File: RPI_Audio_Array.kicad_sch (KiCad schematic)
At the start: 74 parts, among them J1 Conn_02x20_Odd_Even, U1 PCMD3140IRTER, U2 SPH0690LM4H-1, U3 SPH0690LM4H-1, U4 SPH0690LM4H-1, U5 SPH0690LM4H-1, U6 TLV7103318QDSERQ1

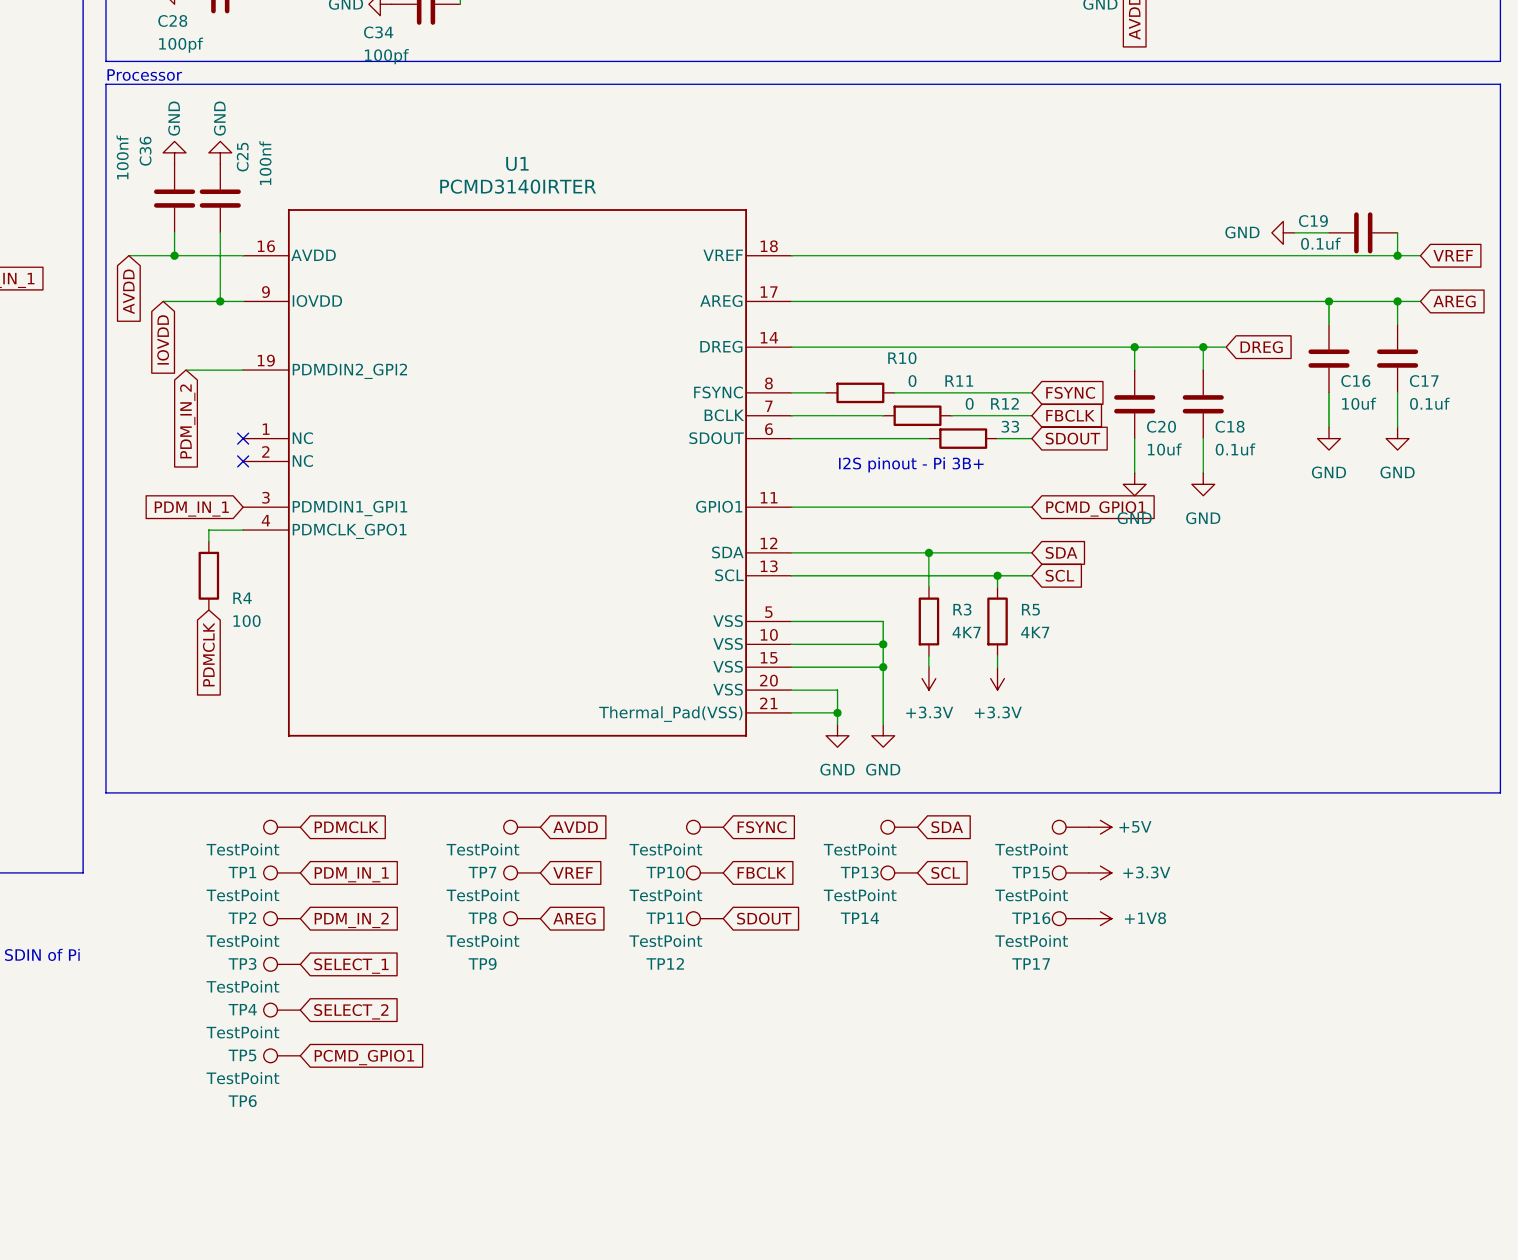
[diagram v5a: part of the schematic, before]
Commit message: Feat: Resolving all DRC warnings
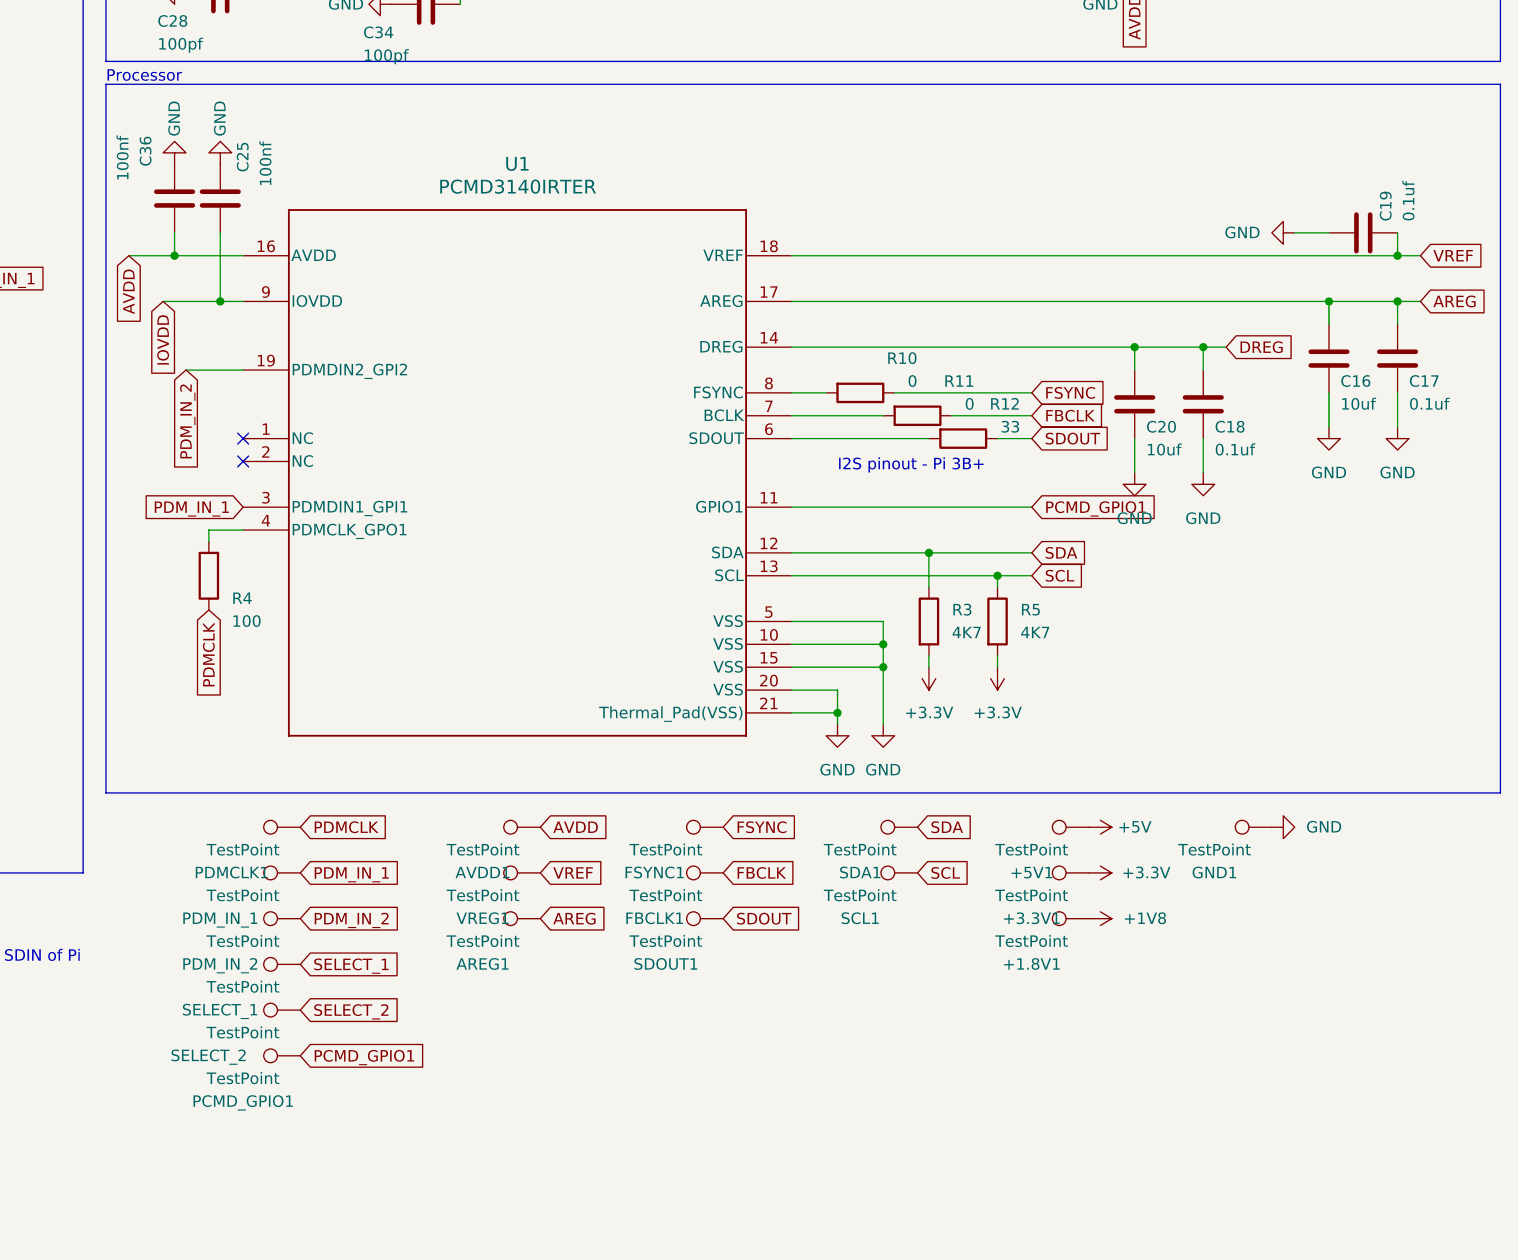
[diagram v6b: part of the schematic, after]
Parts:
- added GND1: TestPoint, TestPoint:TestPoint_Plated_Hole_D2.0mm, symbol Connector:TestPoint
- C13, C32: footprint Capacitor_SMD:C_01005_0402Metric -> Capacitor_SMD:C_0805_2012Metric; lcsc CL05B103KB5NNNC -> CL21B103KBANNNC
- C19: footprint Capacitor_SMD:C_01005_0402Metric -> Capacitor_SMD:C_0603_1608Metric; lcsc CL05B104KB54PNC -> CC0603KRX7R9BB104
- renumbered TP17 to +1.8V1, TP16 to +3.3V1, TP15 to +5V1, TP9 to AREG1, TP7 to AVDD1, TP11 to FBCLK1, TP10 to FSYNC1, TP6 to PCMD_GPIO1, TP1 to PDMCLK1, TP2 to PDM_IN_1, TP3 to PDM_IN_2, TP14 to SCL1, TP13 to SDA1, TP12 to SDOUT1, TP4 to SELECT_1, TP5 to SELECT_2, TP8 to VREG1
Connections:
- net GND: now also GND1.1

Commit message: updated PCB and schematic for review
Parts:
- removed +1.8V1, +3.3V1, +5V1, AREG1, AVDD1, FBCLK1, FSYNC1, GND1, PCMD_GPIO1, PDMCLK1, PDM_IN_1, PDM_IN_2, SCL1, SDA1, SDOUT1, SELECT_1, SELECT_2, VREG1: TestPoint, TestPoint:TestPoint_Plated_Hole_D2.0mm, symbol Connector:TestPoint
- removed C36: 100nf, Capacitor_SMD:C_1206_3216Metric, symbol Device:C
- added C35: 100nF, Capacitor_SMD:C_0603_1608Metric, symbol Device:C
- added H1, H2: MountingHole, MountingHole:MountingHole_2.7mm_M2.5, symbol Mechanical:MountingHole
- added TP1: PDMCLK, TestPoint:TestPoint_Plated_Hole_D2.0mm, symbol Connector:TestPoint
- added TP10: FSYNC, TestPoint:TestPoint_Plated_Hole_D2.0mm, symbol Connector:TestPoint
- added TP11: FBCLK, TestPoint:TestPoint_Plated_Hole_D2.0mm, symbol Connector:TestPoint
- added TP12: SDOUT, TestPoint:TestPoint_Plated_Hole_D2.0mm, symbol Connector:TestPoint
- added TP13: SDA, TestPoint:TestPoint_Plated_Hole_D2.0mm, symbol Connector:TestPoint
- added TP14: SCL, TestPoint:TestPoint_Plated_Hole_D2.0mm, symbol Connector:TestPoint
- added TP15: 5V, TestPoint:TestPoint_Plated_Hole_D2.0mm, symbol Connector:TestPoint
- added TP16: 3V3, TestPoint:TestPoint_Plated_Hole_D2.0mm, symbol Connector:TestPoint
- added TP17: 1V8, TestPoint:TestPoint_Plated_Hole_D2.0mm, symbol Connector:TestPoint
- added TP18: GND, TestPoint:TestPoint_Plated_Hole_D2.0mm, symbol Connector:TestPoint
- added TP19: PDMVDD3, TestPoint:TestPoint_Plated_Hole_D2.0mm, symbol Connector:TestPoint
- added TP2: PDMIN1, TestPoint:TestPoint_Plated_Hole_D2.0mm, symbol Connector:TestPoint
- added TP20: PDMVDD4, TestPoint:TestPoint_Plated_Hole_D2.0mm, symbol Connector:TestPoint
- added TP3: PDMIN2, TestPoint:TestPoint_Plated_Hole_D2.0mm, symbol Connector:TestPoint
- added TP4, TP5: PDMVDD2, TestPoint:TestPoint_Plated_Hole_D2.0mm, symbol Connector:TestPoint
- added TP6: PCM_IO1, TestPoint:TestPoint_Plated_Hole_D2.0mm, symbol Connector:TestPoint
- added TP8: VREF, TestPoint:TestPoint_Plated_Hole_D2.0mm, symbol Connector:TestPoint
- added TP9: AREG, TestPoint:TestPoint_Plated_Hole_D2.0mm, symbol Connector:TestPoint
- C1, C17, C18, C19, C2, C4, C6: value 0.1uf -> 100nF; lcsc CC0603KRX7R9BB104 -> C14663
- C10, C3, C7, C9: value 47pf -> 47pF; lcsc CL10C470JB8NNNC -> C1671
- C11, C12, C5, C8: value 330pf -> 330pF; lcsc CL10C331JB8NNNC -> C1664
- C13, C32: value 10nf -> 10nF; footprint Capacitor_SMD:C_0805_2012Metric -> Capacitor_SMD:C_0603_1608Metric; lcsc CL21B103KBANNNC -> C57112
- C14, C15: value 1uf -> 1uF; lcsc CL10A105KB8NNNC -> C15849
- C16, C20: value 10uf -> 10uF; lcsc CL21A106KAYNNNE -> C440198
- C21, C22, C23, C24: value 2.2uf -> 2.2uF; lcsc CL21A225KBQNNNE -> C377773
- C25, C26, C31: value 100nf -> 100nF; footprint Capacitor_SMD:C_1206_3216Metric -> Capacitor_SMD:C_0603_1608Metric; lcsc CL31B104KBCNNNC -> C14663
- C27, C33: value 1nf -> 1nF; footprint Capacitor_SMD:C_0805_2012Metric -> Capacitor_SMD:C_0603_1608Metric; lcsc CL21B102KBCNNNC -> C1588
- C28, C34: value 100pf -> 100pF; footprint Capacitor_SMD:C_0805_2012Metric -> Capacitor_SMD:C_0603_1608Metric; lcsc CL21C101JBANNNC -> C14858
- C29, C30: value 10uf -> 10uF; lcsc CL31A106KBHNNNE -> C13585
- FB1, FB2, FB3, FB4, FB5: footprint Capacitor_SMD:C_0805_2012Metric -> Inductor_SMD:L_0805_2012Metric; lcsc GZ2012D601TF -> C1017
- J1: lcsc (none) -> DNP
- R1, R2, R4, R8, R9: value 100 -> 100Ω; footprint Resistor_SMD:R_1206_3216Metric -> Resistor_SMD:R_0603_1608Metric; lcsc 1206W4F1000T5E -> C22775
- R10, R11: value 0 -> 0Ω; footprint Resistor_SMD:R_1206_3216Metric -> Resistor_SMD:R_0603_1608Metric; lcsc 1206W4F0000T5E -> C21189
- R12: value 33 -> 33Ω; footprint Resistor_SMD:R_0805_2012Metric -> Resistor_SMD:R_0603_1608Metric; lcsc 0805W8F330JT5E -> C23140
- R3, R5: value 4K7 -> 4K7Ω; lcsc 0603WAF4701T5E -> C23162
- U1: footprint RTE0020A-MFG -> Audio_Break_Out:RTE0020A-MFG; lcsc (none) -> DNP (Not Available)
- U2, U3, U4, U5: footprint SPH0690LM4H-1_KNO -> Audio_Break_Out:SPH0690LM4H-1_KNO; lcsc PCMD3140IRTER -> DNP (Not Available)
- U6: lcsc TLV7103318QDSERQ1 -> DNP (Not Available)
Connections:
- net +1V8: now also C13.1, C14.1, C26.1, C27.1, C28.1, C29.1, TP17.1; no longer C15.1, C30.1, C31.1, C32.1, C33.1, C34.1
- net +5V: now also TP15.1
- net AREG: now also TP9.1
- net FBCLK: now also TP11.1
- net FSYNC: now also TP10.1
- net GND: now also J1.14 (Pin_14), J1.20 (Pin_20), J1.25 (Pin_25), J1.30 (Pin_30), J1.34 (Pin_34), J1.39 (Pin_39), J1.6 (Pin_6), J1.9 (Pin_9), U1.V (Thermal_Pad(VSS)), C35.2, TP18.1
- net PCMD_GPIO1: now also TP6.1
- net PDMCLK: now also TP1.1
- net PDM_IN_1: now also TP2.1
- net PDM_IN_2: now also TP3.1
- net SCL: now also TP14.1
- net SDA: now also TP13.1
- net SDOUT: now also TP12.1
- net VREF: now also TP8.1
- net PDM_VDD2: now reaches C2.1, C23.1, C3.1, C5.1, FB3.1, U3.5 (VDD)
- net PDM_VDD2: now also TP5.1
- net PDM_VDD4: now reaches C10.1, C12.1, C21.1, C4.1, FB5.1, U5.5 (VDD)
- net PDM_VDD4: now also TP20.1
- net +3.3V renamed +3V3
- net +3V3: now also C15.1, C30.1, C31.1, C32.1, C33.1, C34.1, FB1.2, U1.16 (AVDD), C35.1, TP16.1; no longer FB1.1, U6.6 (OUT1)
- removed net AVDD: C13.1, C14.1, C26.1, C27.1, C28.1, C29.1, FB1.2, U1.16 (AVDD)
- net SELECT_1 renamed PDM_VDD3
- net PDM_VDD3: now also TP19.1
- net SELECT_2 renamed PDM_VDD1
- net PDM_VDD1: now also TP4.1
- new net: FB1.1, U6.6 (OUT1)
- no-connect marks 39 -> 31
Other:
- moved on the sheet: C13, C14, C15, C26, C27, C28, C29, C30, C31, C32, C33, C34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
